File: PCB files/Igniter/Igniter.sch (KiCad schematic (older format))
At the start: 22 parts, among them J2 Battery, J3 PT2, J4 PT1, J5 PT3, J6 PT4, J7 IgnitionCoil, Q1 N MOSFET, SW1 ARM

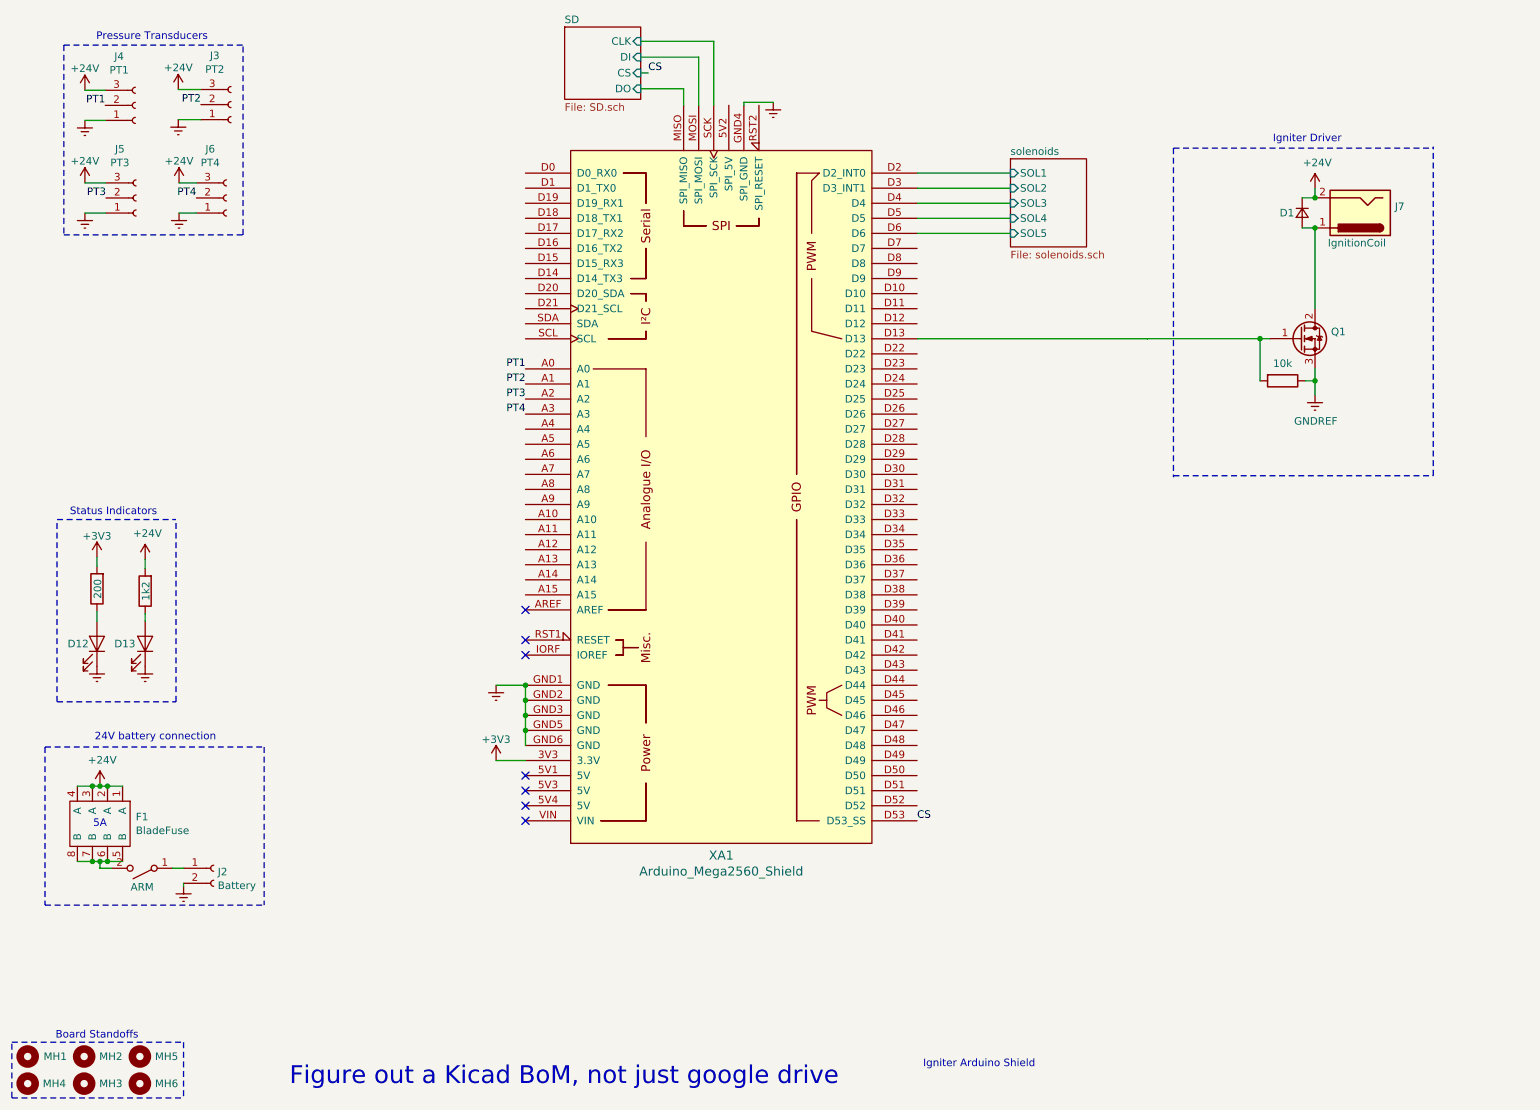
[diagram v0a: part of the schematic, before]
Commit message: 12/4/2019
Changed P transducers connector to dsub
Moved SD card circuit onto main shematic sheet
😂
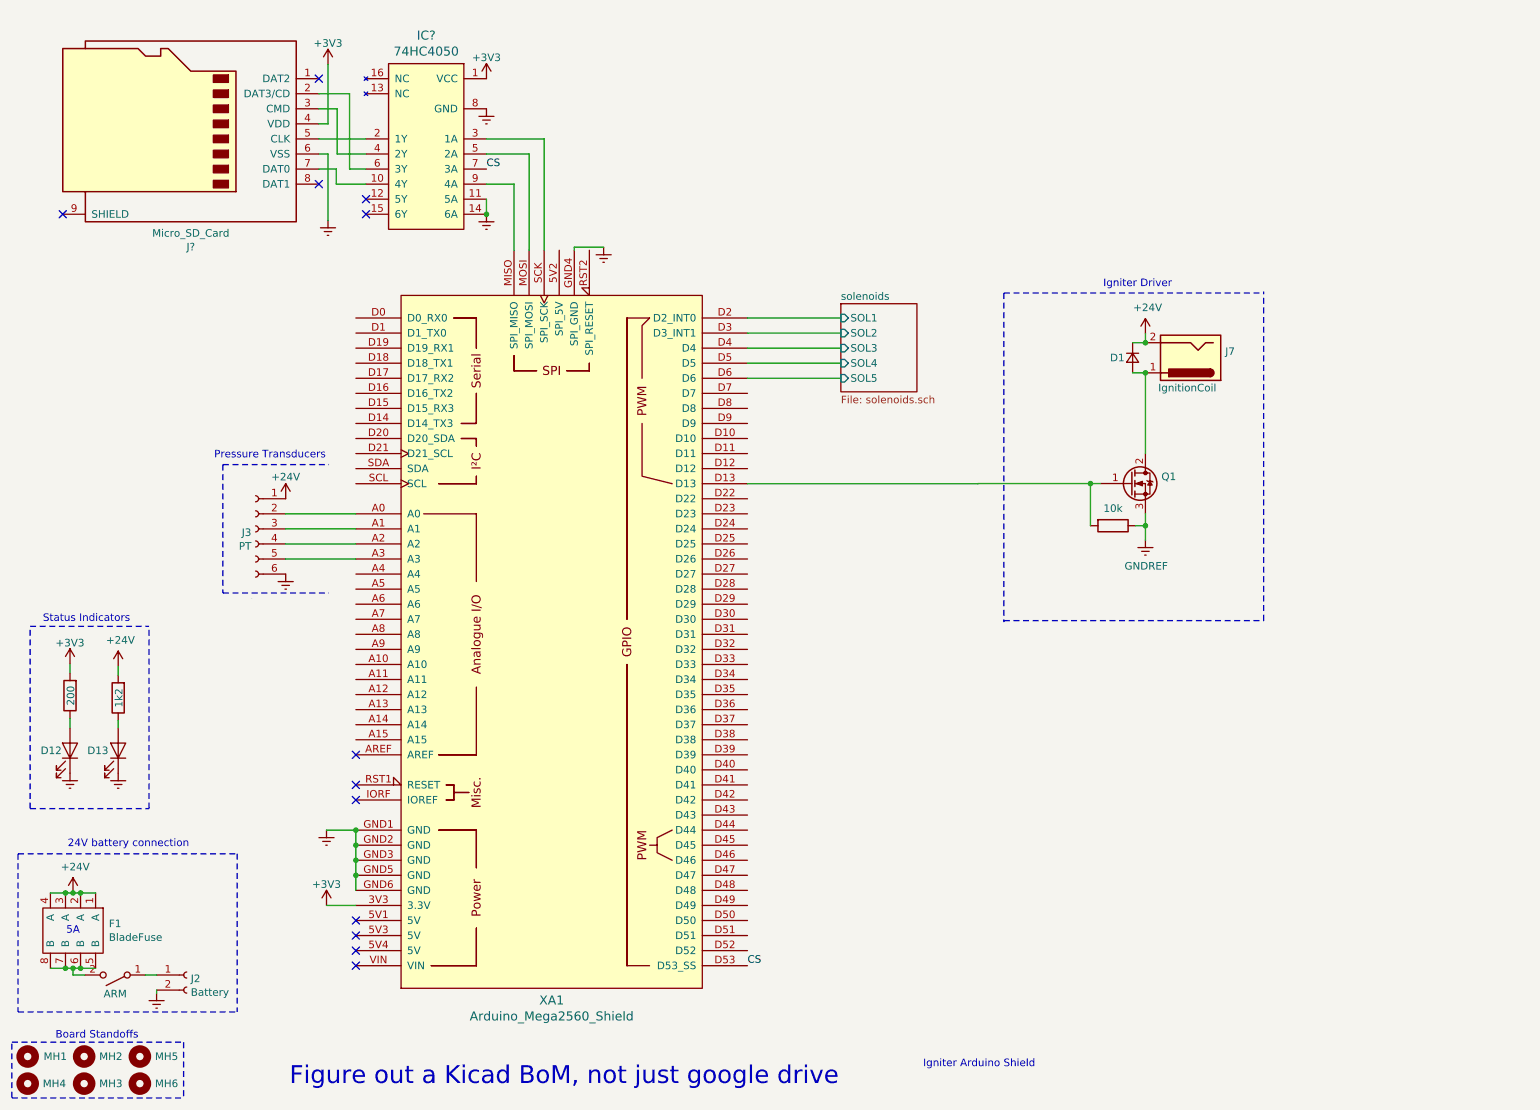
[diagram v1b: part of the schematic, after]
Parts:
- removed J3: PT2, Connector_Molex:Molex_Mini-Fit_Jr_5566-04A_2x02_P4.20mm_Vertical, symbol Connector:Conn_01x03_Female
- removed J4: PT1, Connector_Molex:Molex_Mini-Fit_Jr_5566-04A_2x02_P4.20mm_Vertical, symbol Connector:Conn_01x03_Female
- removed J5: PT3, Connector_Molex:Molex_Mini-Fit_Jr_5566-04A_2x02_P4.20mm_Vertical, symbol Connector:Conn_01x03_Female
- removed J6: PT4, Connector_Molex:Molex_Mini-Fit_Jr_5566-04A_2x02_P4.20mm_Vertical, symbol Connector:Conn_01x03_Female
- added IC?: 74HC4050, Package_SO:SOP-16_4.4x10.4mm_P1.27mm, symbol Igniter-rescue:74HC4050-7400-ic
- added J3: PT, Connector_Dsub:DSUB-9_Male_Horizontal_P2.77x2.54mm_EdgePinOffset9.40mm, symbol Connector:Conn_01x06_Female
- added J?: Micro_SD_Card, Connector_Card:microSD_HC_Hirose_DM3BT-DSF-PEJS, symbol Igniter-rescue:Micro_SD_Card-Connector
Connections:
- net +24V: now also J3.1 (Pin_1)
- net +3V3: now also IC?.1 (VCC), J?.4 (VDD)
- net CS: now also IC?.7 (3A)
- net GNDREF: now also IC?.11 (5A), IC?.14 (6A), IC?.8 (GND), J3.6 (Pin_6), J?.6 (VSS)
- net PT1: no longer names the net of XA1.A0
- net PT1: now also J3.2 (Pin_2)
- net PT2: no longer names the net of XA1.A1
- net PT2: now also J3.3 (Pin_3)
- net PT3: no longer names the net of XA1.A2
- net PT3: now also J3.4 (Pin_4)
- net PT4: no longer names the net of XA1.A3
- net PT4: now also J3.5 (Pin_5)
- net SD/CLK: no longer names the net of XA1.SCK (SPI_SCK)
- net SD/CLK: now also IC?.3 (1A)
- net SD/DI: no longer names the net of XA1.MOSI (SPI_MOSI)
- net SD/DI: now also IC?.5 (2A)
- net SD/DO: no longer names the net of XA1.MISO (SPI_MISO)
- net SD/DO: now also IC?.9 (4A)
- new net: IC?.10 (4Y), J?.7 (DAT0)
- new net: IC?.2 (1Y), J?.5 (CLK)
- new net: IC?.4 (2Y), J?.3 (CMD)
- new net: IC?.6 (3Y), J?.2 (DAT3/CD)
- no-connect marks 7 -> 12
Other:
- moved on the sheet: D1, D12, D13, F1, J2, J7, Q1, XA1
